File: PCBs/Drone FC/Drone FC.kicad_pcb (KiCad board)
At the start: 4 copper layers, 45.5 x 45.9 mm, 63 parts, among them J1 BATTERY_1S, J2 MOTOR1, J3 MOTOR2, J4 MOTOR3, J5 MOTOR4, J6 SWD_HEADER, J7 CHARGE_PORT, Q1 SI2300, Q2 SI2300, Q3 SI2300, Q4 SI2300, SW1 SLIDE_SWITCH, U1 AMS1117-3.3, U2 STM32F103C8T6, U3 MPU-6050, U4 BK2423, Y1 16MHz, Y2 16MHz

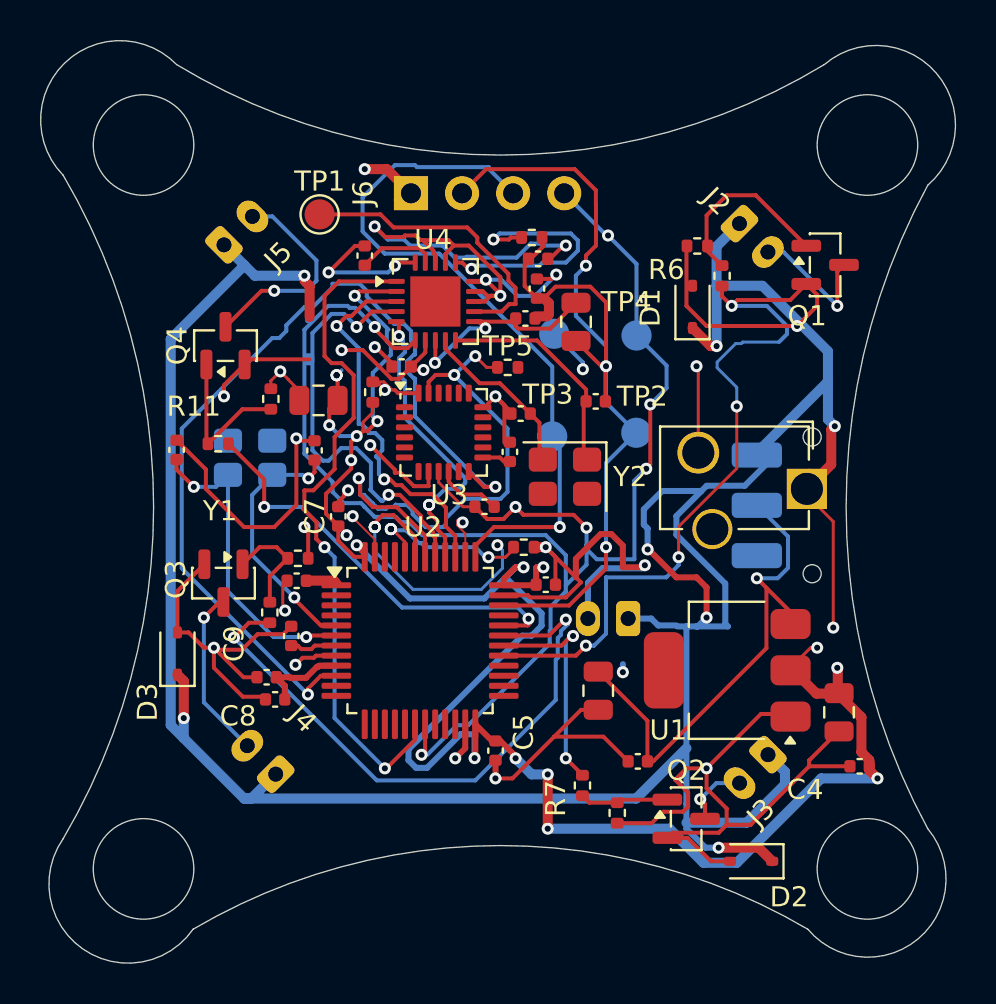
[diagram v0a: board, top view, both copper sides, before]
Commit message: added fixed PCBs
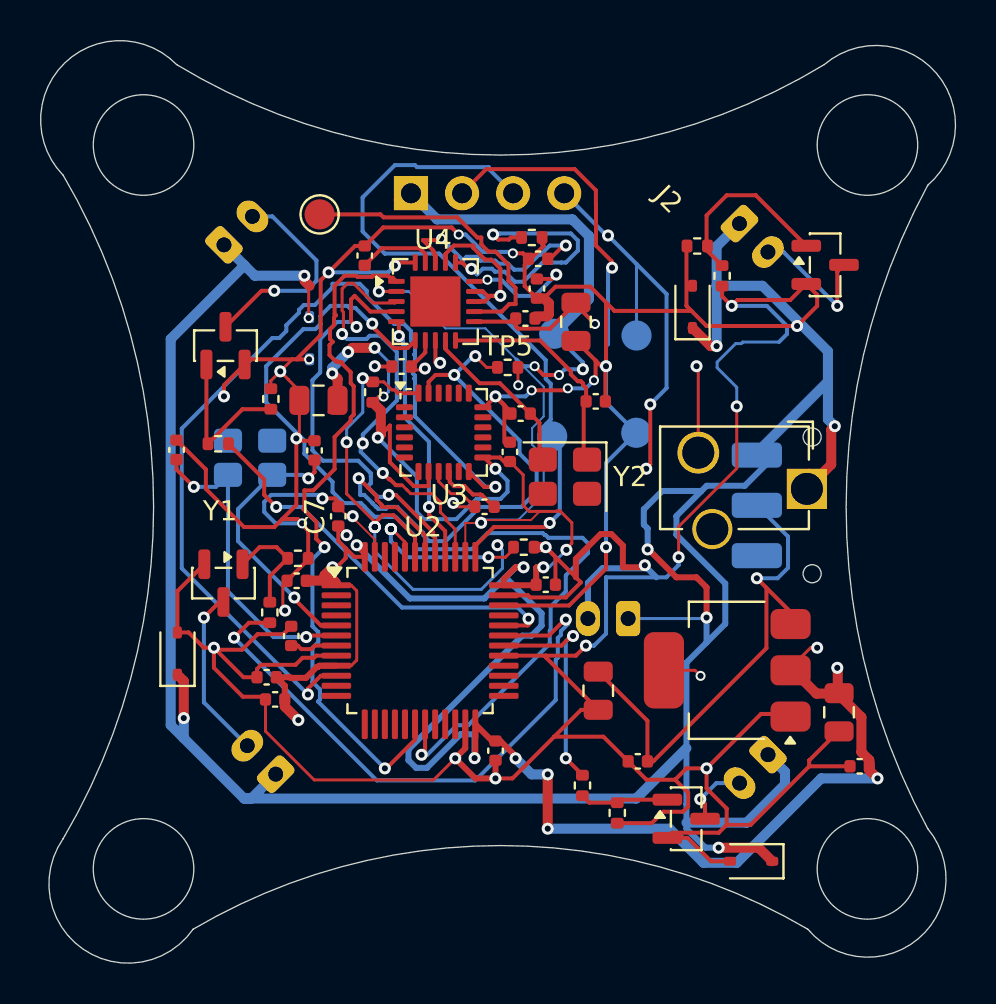
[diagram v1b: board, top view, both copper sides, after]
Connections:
- C10 pad 1: +3.3V -> /RF_CSN
- C11 pad 1: +3.3V -> /RF_CSN
- C14 pad 1: +3.3V -> /RF_CSN
- C19 pad 1: +3.3V -> /RF_CSN
- C3 pad 1: +3.3V -> /RF_CSN
- C4 pad 1: +3.3V -> /RF_CSN
- C5 pad 1: +3.3V -> /RF_CSN
- C6 pad 1: +3.3V -> /RF_CSN
- C7 pad 1: +3.3V -> /RF_CSN
- C8 pad 1: +3.3V -> /RF_CSN
- J6 pad 1: +3.3V -> /RF_CSN
- R2 pad 1: +3.3V -> /RF_CSN
- TP5 pad 1: +3.3V -> /RF_CSN
- U2 pad 1: +3.3V -> /RF_CSN
- U2 pad 24: +3.3V -> /RF_CSN
- U2 pad 36: +3.3V -> /RF_CSN
- U2 pad 48: +3.3V -> /RF_CSN
- U2 pad 9: +3.3V -> /RF_CSN
- U3 pad 13: +3.3V -> /RF_CSN
- U3 pad 8: +3.3V -> /RF_CSN
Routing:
- net /MOTOR1_PWM: track 190.0 -> 251.8 mm, vias 23 -> 28
- net GND: track 4.34 -> 38.6 mm, vias 4 -> 8
- net /RF_IRQ: track 80.1 -> 48.7 mm, vias 5 -> 2
- net /RF_CSN: track 153.2 -> 177.6 mm
- net +3.3V: track 18.5 -> 30.1 mm, vias 7 -> 8
- net /IMU_SDA: track 16.9 -> 25.2 mm, vias 5 -> 6
- net +BATT: track 154.2 -> 146.6 mm
- net /RF_SCK: track 19.0 -> 22.8 mm, vias 2 -> 3
- net /RF_MISO: track 14.9 -> 12.7 mm, vias 3 -> 2
- net /IMU_SCL: track 28.0 -> 30.0 mm
- net /RF_CE: track 34.1 -> 35.0 mm
- net Net-(U4-IREF): track 13.0 -> 13.8 mm
- net /XTAL_IN: track 13.0 -> 13.6 mm
